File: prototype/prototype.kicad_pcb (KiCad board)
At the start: 4 copper layers, 78.7 x 63.5 mm, 47 parts, among them P1 CONN_25X2, P2 CONN_25X2, P3 VGACONN, U1 MC68SEC000, U2 FLASHROM_512K_16, U3 RAM_512K_16, U4 RAM_512K_16

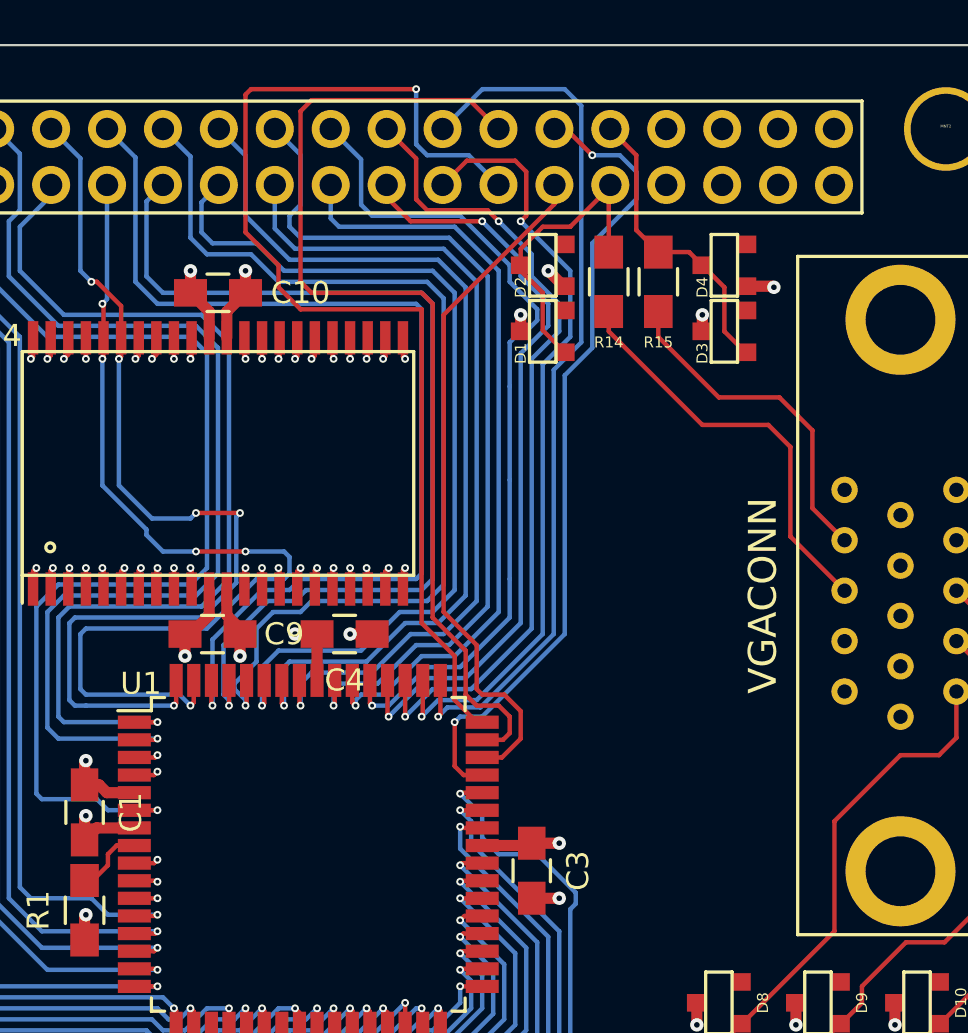
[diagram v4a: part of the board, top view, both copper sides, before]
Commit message: More 68000 signal traces.
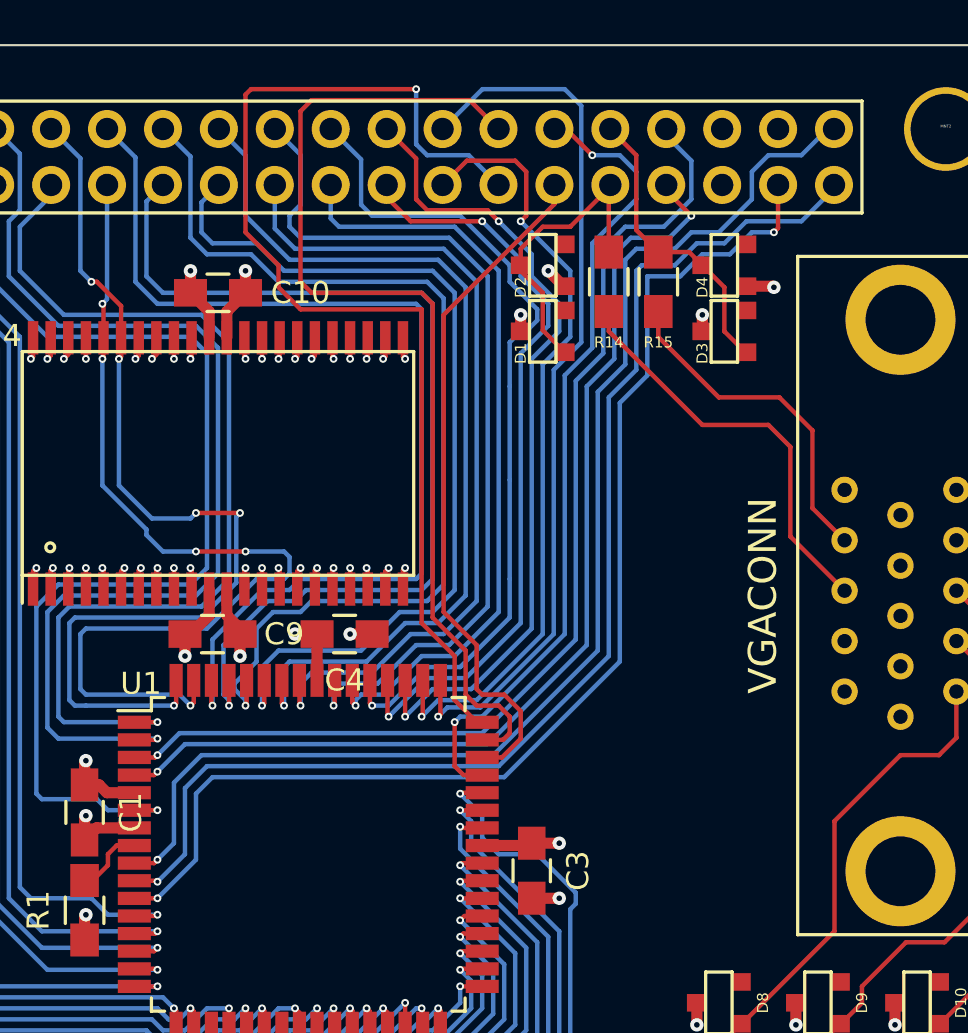
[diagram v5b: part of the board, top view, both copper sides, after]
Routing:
- net ~HALT: track 1.11 -> 57.6 mm
- net ~RESET: track 1.07 -> 56.3 mm
- net ~AVEC: track 1.05 -> 55.1 mm, vias 1 -> 2
- net ~BG: track 1.09 -> 49.1 mm
- net ~BR: track 1.11 -> 47.4 mm, vias 1 -> 2
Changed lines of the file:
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@@
   (general
     (links 270)
-    (no_connects 130)
+    (no_connects 125)
     (area 112.344999 60.909999 191.185001 124.510001)
     (thickness 1.6)
     (drawings 9)
-    (tracks 1453)
+    (tracks 1527)
     (zones 0)
     (modules 47)
@@
   (via (at 150.515 75.21) (size 0.3556) (layers F.Cu B.Cu) (net 80))
   (segment (start 150.665 75.06) (end 150.515 75.21) (width 0.2032) (layer F.Cu) (net 80))
+  (segment (start 174.625 67.31) (end 174.625 67.57) (width 0.2032) (layer F.Cu) (net 81) (status C00000))
+  (segment (start 174.625 67.57) (end 175.765 68.71) (width 0.2032) (layer F.Cu) (net 81) (status 400000))
+  (via (at 175.765 68.71) (size 0.3556) (layers F.Cu B.Cu) (net 81))
+  (segment (start 175.765 68.71) (end 174.765 69.71) (width 0.2032) (layer B.Cu) (net 81))
+  (segment (start 174.765 69.71) (end 173.015 69.71) (width 0.2032) (layer B.Cu) (net 81))
+  (segment (start 173.015 69.71) (end 172.265 70.46) (width 0.2032) (layer B.Cu) (net 81))
+  (segment (start 172.265 70.46) (end 172.265 75.21) (width 0.2032) (layer B.Cu) (net 81))
+  (segment (start 172.265 75.21) (end 171.015 76.46) (width 0.2032) (layer B.Cu) (net 81))
+  (segment (start 171.015 76.46) (end 171.015 88.21) (width 0.2032) (layer B.Cu) (net 81))
+  (segment (start 171.015 88.21) (end 166.515 92.71) (width 0.2032) (layer B.Cu) (net 81))
+  (segment (start 166.515 92.71) (end 152.765 92.71) (width 0.2032) (layer B.Cu) (net 81))
+  (segment (start 152.765 92.71) (end 151.515 93.96) (width 0.2032) (layer B.Cu) (net 81))
   (segment (start 150.465 94.115) (end 151.36 94.115) (width 0.2032) (layer F.Cu) (net 81))
   (via (at 151.515 93.96) (size 0.3556) (layers F.Cu B.Cu) (net 81))
   (segment (start 151.36 94.115) (end 151.515 93.96) (width 0.2032) (layer F.Cu) (net 81))
+  (segment (start 174.625 64.77) (end 174.625 65.07) (width 0.2032) (layer B.Cu) (net 82) (status C00000))
+  (segment (start 174.625 65.07) (end 175.765 66.21) (width 0.2032) (layer B.Cu) (net 82) (status 400000))
+  (segment (start 175.765 66.21) (end 175.765 67.96) (width 0.2032) (layer B.Cu) (net 82))
+  (segment (start 175.765 67.96) (end 174.515 69.21) (width 0.2032) (layer B.Cu) (net 82))
+  (segment (start 174.515 69.21) (end 172.765 69.21) (width 0.2032) (layer B.Cu) (net 82))
+  (segment (start 172.765 69.21) (end 171.765 70.21) (width 0.2032) (layer B.Cu) (net 82))
+  (segment (start 171.765 70.21) (end 171.765 74.96) (width 0.2032) (layer B.Cu) (net 82))
+  (segment (start 171.765 74.96) (end 170.515 76.21) (width 0.2032) (layer B.Cu) (net 82))
+  (segment (start 170.515 76.21) (end 170.515 87.96) (width 0.2032) (layer B.Cu) (net 82))
+  (segment (start 170.515 87.96) (end 166.265 92.21) (width 0.2032) (layer B.Cu) (net 82))
+  (segment (start 166.265 92.21) (end 152.515 92.21) (width 0.2032) (layer B.Cu) (net 82))
+  (segment (start 152.515 92.21) (end 151.515 93.21) (width 0.2032) (layer B.Cu) (net 82))
   (segment (start 150.465 93.315) (end 151.41 93.315) (width 0.2032) (layer F.Cu) (net 82))
   (via (at 151.515 93.21) (size 0.3556) (layers F.Cu B.Cu) (net 82))
@@
   (via (at 150.015 84.71) (size 0.3556) (layers F.Cu B.Cu) (net 84))
   (segment (start 149.865 84.86) (end 150.015 84.71) (width 0.2032) (layer F.Cu) (net 84))
-  (segment (start 150.465 99.715) (end 151.51 99.715) (width 0.2032) (layer F.Cu) (net 85))
-  (via (at 151.515 99.71) (size 0.3556) (layers F.Cu B.Cu) (net 85))
+  (segment (start 179.705 67.31) (end 179.705 69.27) (width 0.2032) (layer F.Cu) (net 85) (status 400000))
   (segment (start 151.51 99.715) (end 151.515 99.71) (width 0.2032) (layer F.Cu) (net 85))
+  (via (at 151.515 99.71) (size 0.3556) (layers F.Cu B.Cu) (net 85))
+  (segment (start 151.51 99.715) (end 150.465 99.715) (width 0.2032) (layer F.Cu) (net 85))
+  (segment (start 153.265 97.96) (end 151.515 99.71) (width 0.2032) (layer B.Cu) (net 85))
+  (segment (start 153.265 94.96) (end 153.265 97.96) (width 0.2032) (layer B.Cu) (net 85))
+  (segment (start 154.015 94.21) (end 153.265 94.96) (width 0.2032) (layer B.Cu) (net 85))
+  (segment (start 167.265 94.21) (end 154.015 94.21) (width 0.2032) (layer B.Cu) (net 85))
+  (segment (start 172.515 88.96) (end 167.265 94.21) (width 0.2032) (layer B.Cu) (net 85))
+  (segment (start 172.515 77.21) (end 172.515 88.96) (width 0.2032) (layer B.Cu) (net 85))
+  (segment (start 173.765 75.96) (end 172.515 77.21) (width 0.2032) (layer B.Cu) (net 85))
+  (segment (start 173.765 71.46) (end 173.765 75.96) (width 0.2032) (layer B.Cu) (net 85))
+  (segment (start 175.265 71.46) (end 173.765 71.46) (width 0.2032) (layer B.Cu) (net 85))
+  (segment (start 176.265 70.46) (end 175.265 71.46) (width 0.2032) (layer B.Cu) (net 85))
+  (segment (start 177.515 70.46) (end 176.265 70.46) (width 0.2032) (layer B.Cu) (net 85))
+  (segment (start 178.515 69.46) (end 177.515 70.46) (width 0.2032) (layer B.Cu) (net 85))
+  (segment (start 179.515 69.46) (end 178.515 69.46) (width 0.2032) (layer B.Cu) (net 85))
+  (via (at 179.515 69.46) (size 0.3556) (layers F.Cu B.Cu) (net 85))
+  (segment (start 179.705 69.27) (end 179.515 69.46) (width 0.2032) (layer F.Cu) (net 85))
   (segment (start 115.37 111.05) (end 115.37 109.815) (width 0.2032) (layer F.Cu) (net 86))
   (via (at 115.265 109.71) (size 0.3556) (layers F.Cu B.Cu) (net 86))
   (segment (start 115.37 109.815) (end 115.265 109.71) (width 0.2032) (layer F.Cu) (net 86))
+  (segment (start 182.245 67.31) (end 182.245 67.48) (width 0.2032) (layer B.Cu) (net 87) (status C00000))
+  (segment (start 182.245 67.48) (end 180.765 68.96) (width 0.2032) (layer B.Cu) (net 87) (status 400000))
+  (segment (start 180.765 68.96) (end 178.265 68.96) (width 0.2032) (layer B.Cu) (net 87))
+  (segment (start 178.265 68.96) (end 177.265 69.96) (width 0.2032) (layer B.Cu) (net 87))
+  (segment (start 177.265 69.96) (end 176.015 69.96) (width 0.2032) (layer B.Cu) (net 87))
+  (segment (start 176.015 69.96) (end 175.015 70.96) (width 0.2032) (layer B.Cu) (net 87))
+  (segment (start 175.015 70.96) (end 173.515 70.96) (width 0.2032) (layer B.Cu) (net 87))
+  (segment (start 173.515 70.96) (end 173.265 71.21) (width 0.2032) (layer B.Cu) (net 87))
+  (segment (start 173.265 71.21) (end 173.265 75.71) (width 0.2032) (layer B.Cu) (net 87))
+  (segment (start 173.265 75.71) (end 172.015 76.96) (width 0.2032) (layer B.Cu) (net 87))
+  (segment (start 172.015 76.96) (end 172.015 88.71) (width 0.2032) (layer B.Cu) (net 87))
+  (segment (start 172.015 88.71) (end 167.015 93.71) (width 0.2032) (layer B.Cu) (net 87))
+  (segment (start 167.015 93.71) (end 153.765 93.71) (width 0.2032) (layer B.Cu) (net 87))
+  (segment (start 153.765 93.71) (end 152.765 94.71) (width 0.2032) (layer B.Cu) (net 87))
+  (segment (start 152.765 94.71) (end 152.765 97.71) (width 0.2032) (layer B.Cu) (net 87))
+  (segment (start 152.765 97.71) (end 151.515 98.96) (width 0.2032) (layer B.Cu) (net 87))
   (segment (start 150.465 98.915) (end 151.47 98.915) (width 0.2032) (layer F.Cu) (net 87))
   (via (at 151.515 98.96) (size 0.3556) (layers F.Cu B.Cu) (net 87))
   (segment (start 151.47 98.915) (end 151.515 98.96) (width 0.2032) (layer F.Cu) (net 87))
+  (segment (start 182.245 64.77) (end 181.955 64.77) (width 0.2032) (layer B.Cu) (net 88) (status C00000))
+  (segment (start 181.955 64.77) (end 180.765 65.96) (width 0.2032) (layer B.Cu) (net 88) (status 400000))
+  (segment (start 180.765 65.96) (end 179.265 65.96) (width 0.2032) (layer B.Cu) (net 88))
+  (segment (start 179.265 65.96) (end 178.515 66.71) (width 0.2032) (layer B.Cu) (net 88))
+  (segment (start 178.515 66.71) (end 178.515 67.96) (width 0.2032) (layer B.Cu) (net 88))
+  (segment (start 178.515 67.96) (end 177.015 69.46) (width 0.2032) (layer B.Cu) (net 88))
+  (segment (start 177.015 69.46) (end 175.765 69.46) (width 0.2032) (layer B.Cu) (net 88))
+  (segment (start 175.765 69.46) (end 175.015 70.21) (width 0.2032) (layer B.Cu) (net 88))
+  (segment (start 175.015 70.21) (end 173.265 70.21) (width 0.2032) (layer B.Cu) (net 88))
+  (segment (start 173.265 70.21) (end 172.765 70.71) (width 0.2032) (layer B.Cu) (net 88))
+  (segment (start 172.765 70.71) (end 172.765 75.46) (width 0.2032) (layer B.Cu) (net 88))
+  (segment (start 172.765 75.46) (end 171.515 76.71) (width 0.2032) (layer B.Cu) (net 88))
+  (segment (start 171.515 76.71) (end 171.515 88.46) (width 0.2032) (layer B.Cu) (net 88))
+  (segment (start 171.515 88.46) (end 166.765 93.21) (width 0.2032) (layer B.Cu) (net 88))
+  (segment (start 166.765 93.21) (end 153.515 93.21) (width 0.2032) (layer B.Cu) (net 88))
+  (segment (start 153.515 93.21) (end 152.265 94.46) (width 0.2032) (layer B.Cu) (net 88))
+  (segment (start 152.265 94.46) (end 152.265 97.21) (width 0.2032) (layer B.Cu) (net 88))
+  (segment (start 152.265 97.21) (end 151.515 97.96) (width 0.2032) (layer B.Cu) (net 88))
   (segment (start 150.465 98.115) (end 151.36 98.115) (width 0.2032) (layer F.Cu) (net 88))
   (via (at 151.515 97.96) (size 0.3556) (layers F.Cu B.Cu) (net 88))

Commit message: Even more PCB routing.
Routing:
- net A1: track 39.5 -> 69.0 mm

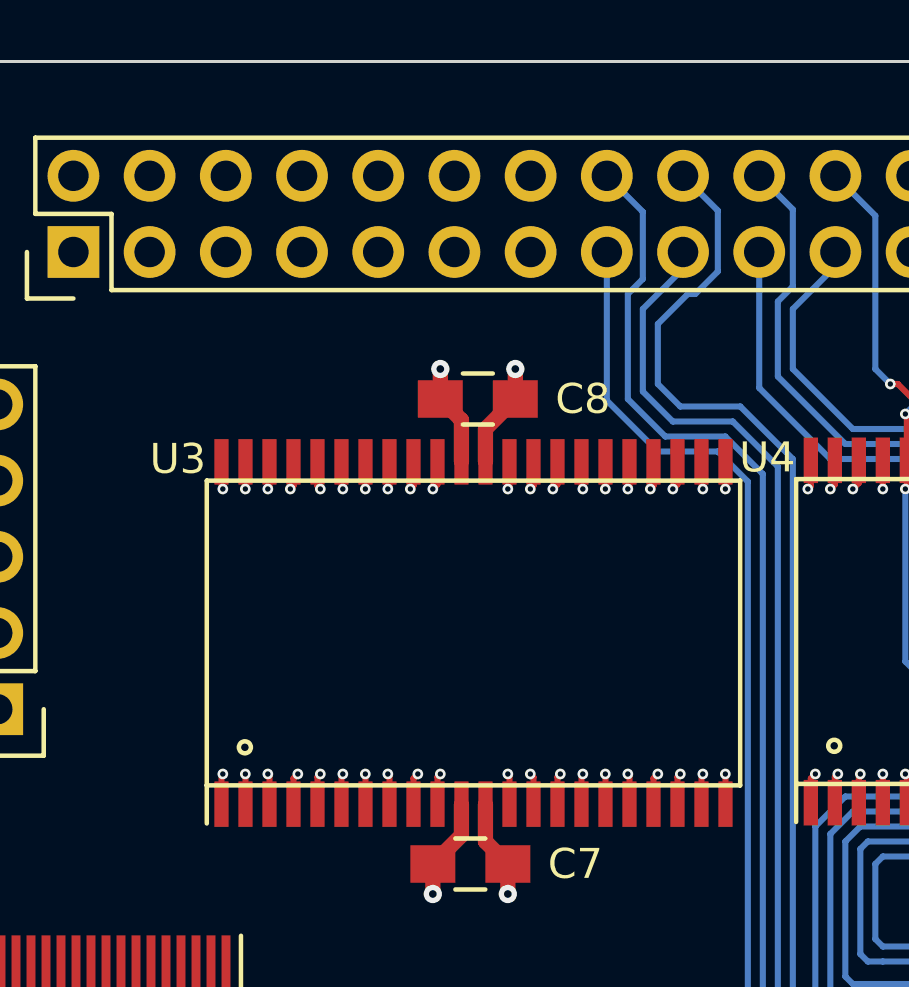
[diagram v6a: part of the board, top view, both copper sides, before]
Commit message: A tangled mess of traces for physical addresses and one RAM.
Will probably need to tear all this up and try again.
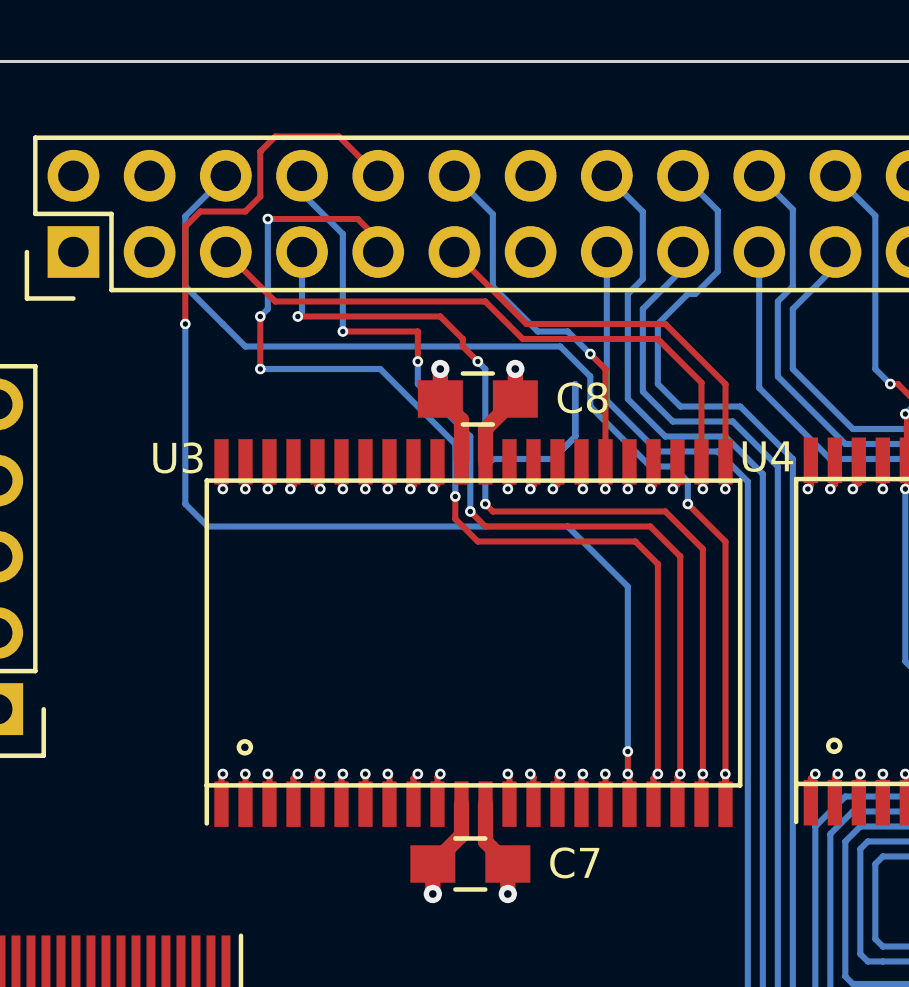
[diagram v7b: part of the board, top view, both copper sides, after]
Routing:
- net PA17: track 3.39 -> 43.9 mm, vias 3 -> 5
- net PA14: track 3.40 -> 42.9 mm, vias 3 -> 6
- net PA13: track 3.36 -> 38.9 mm, vias 3 -> 4
- net PA16: track 3.37 -> 37.3 mm, vias 3 -> 7
- net PA15: track 3.37 -> 33.2 mm, vias 3 -> 6
- net PA12: track 3.27 -> 23.6 mm
- net PA18: track 3.26 -> 16.7 mm
- net PA19: track 3.28 -> 15.5 mm, vias 3 -> 4

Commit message: A few more tangles before I call it a night.
Too late for this nonsense.
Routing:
- net D5: track 43.9 -> 80.0 mm
- net D7: track 41.6 -> 76.4 mm
- net D4: track 41.8 -> 75.9 mm
- net PA17: track 43.9 -> 77.9 mm
- net D6: track 38.7 -> 71.5 mm
